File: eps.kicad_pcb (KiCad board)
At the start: 2 copper layers, 96 x 90 mm, 0 parts

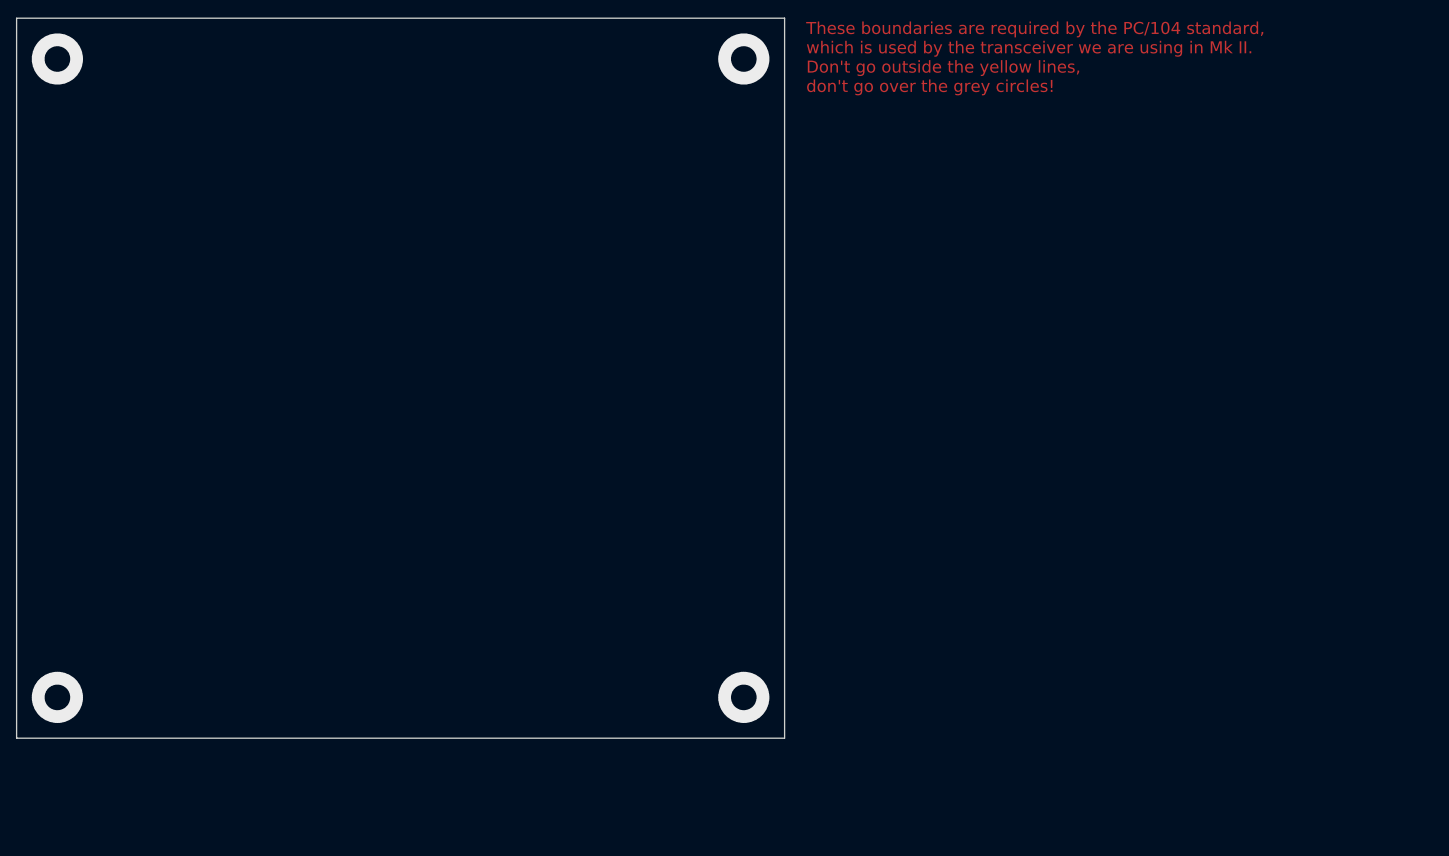
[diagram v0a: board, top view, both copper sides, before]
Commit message: PCB layout as of 2018-02-12
All that’s left to do is add deployment switches
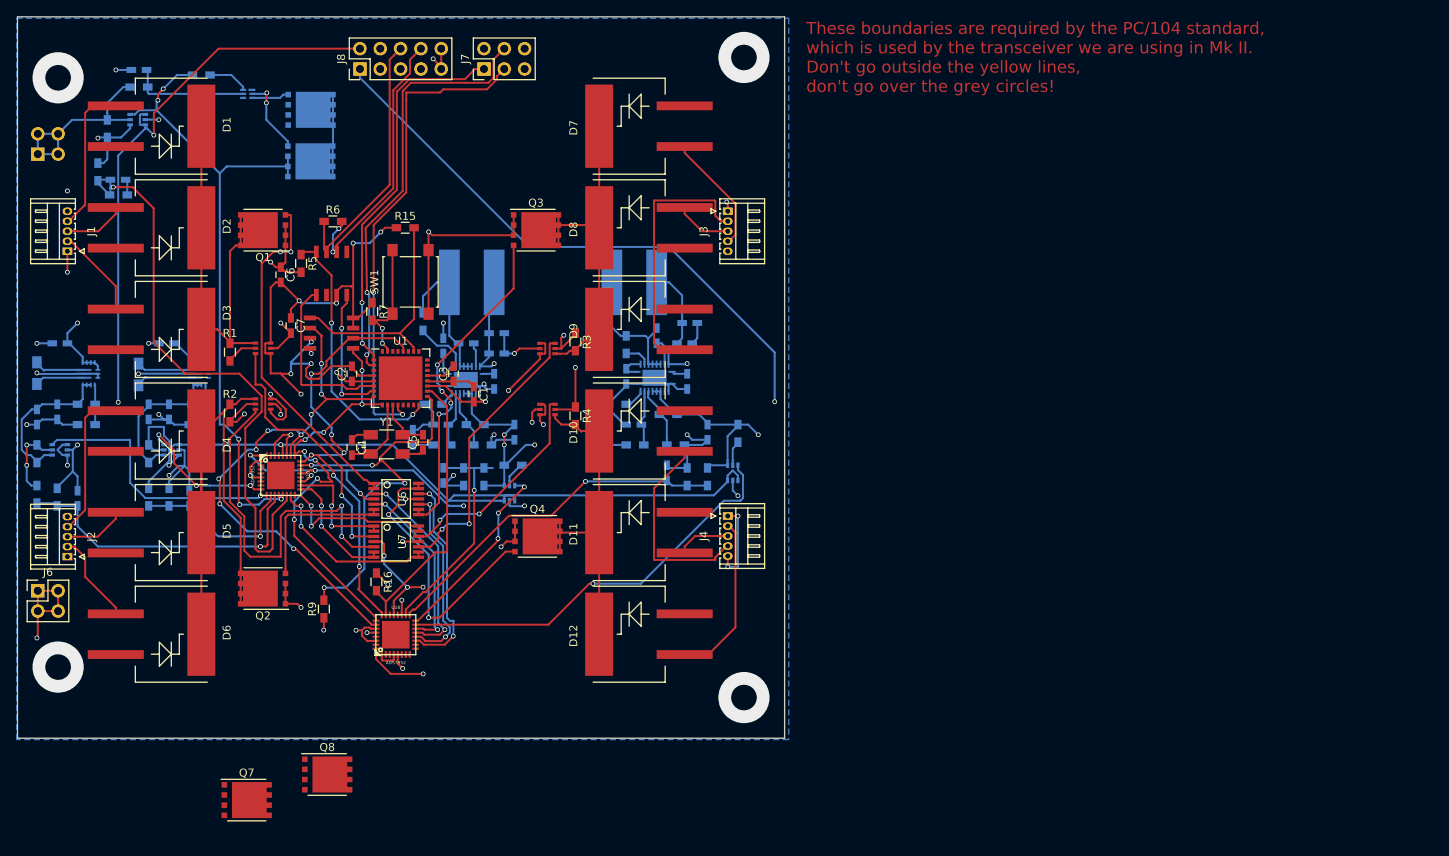
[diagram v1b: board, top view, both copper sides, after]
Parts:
- added C1: 0.1µF, Capacitors_SMD:C_0603_HandSoldering, F.Cu at (157.2, 97.0)
- added C10: C_Small, Capacitors_SMD:C_0603_HandSoldering, B.Cu at (121.6, 110.0)
- added C11: C_Small, Capacitors_SMD:C_0603_HandSoldering, B.Cu at (181.3, 106.8)
- added C12: C_Small, Capacitors_SMD:C_0603_HandSoldering, B.Cu at (153.3, 107.2)
- added C13: C_small, Capacitors_SMD:C_0603_HandSoldering, B.Cu at (112.7, 70.2)
- added C2: 0.1µF, Capacitors_SMD:C_0603_HandSoldering, F.Cu at (141.9, 94.5)
- added C3: 0.1µF, Capacitors_SMD:C_0603_HandSoldering, F.Cu at (154.6, 94.5)
- added C4: 22pF, Capacitors_SMD:C_0603_HandSoldering, F.Cu at (141.9, 103.7)
- added C5: 22pF, Capacitors_SMD:C_0603_HandSoldering, F.Cu at (150.8, 103.0)
- added C6: 0.1µF, Capacitors_SMD:C_0603_HandSoldering, F.Cu at (133.0, 82.1)
- added C7: 100nF, Capacitors_SMD:C_0603_HandSoldering, F.Cu at (134.3, 88.4)
- added C8: 0.1uF, Capacitors_SMD:C_0603_HandSoldering, B.Cu at (115.3, 56.5)
- added C9: C_Small, Capacitors_SMD:C_0603_HandSoldering, B.Cu at (107.6, 110.0)
- added CbstA1: 100nF, Capacitors_SMD:C_0603_HandSoldering, B.Cu at (156.2, 90.6)
- added CbstB1: 100nF, Capacitors_SMD:C_0603_HandSoldering, B.Cu at (180.0, 89.7)
- added Ccomp2A1: 82pF, Capacitors_SMD:C_0603_HandSoldering, B.Cu at (153.0, 100.8)
- added Ccomp2B1: 82pF, Capacitors_SMD:C_0603_HandSoldering, B.Cu at (177.2, 100.8)
- added CcompA1: 1.8nF, Capacitors_SMD:C_0603_HandSoldering, B.Cu at (149.5, 102.4)
- added CcompB1: 1.8nF, Capacitors_SMD:C_0603_HandSoldering, B.Cu at (173.7, 102.4)
- added Cin1: 10.0µF, Capacitors_SMD:C_0603_HandSoldering, B.Cu at (105.4, 90.6)
- added Cin2: 10.0µF, Capacitors_SMD:C_0603_HandSoldering, B.Cu at (118.7, 90.6)
- added Cin2A1: 100n, Capacitors_SMD:C_0603_HandSoldering, B.Cu at (160.0, 89.4)
- added Cin2B1: 100n, Capacitors_SMD:C_0603_HandSoldering, B.Cu at (184.1, 88.1)
- added CinA1: 12µF, Capacitors_SMD:C_0603_HandSoldering, B.Cu at (160.0, 91.9)
- added CinB1: 12µF, Capacitors_SMD:C_0603_HandSoldering, B.Cu at (183.5, 90.6)
- added Cout1: 47.0µF, Capacitors_SMD:C_0603_HandSoldering, B.Cu at (102.5, 99.8)
- added Cout2: 47.0µF, Capacitors_SMD:C_0603_HandSoldering, B.Cu at (116.5, 99.2)
- added CoutA1: 47µF, Capacitors_SMD:C_0603_HandSoldering, B.Cu at (162.2, 101.8)
- added CoutB1: 47µF, Capacitors_SMD:C_0603_HandSoldering, B.Cu at (186.4, 101.8)
- added Coutx1: 10.0µF, Capacitors_SMD:C_0603_HandSoldering, B.Cu at (105.1, 99.2)
- added Coutx2: 10.0µF, Capacitors_SMD:C_0603_HandSoldering, B.Cu at (119.0, 99.2)
- added CssA1: 8.2nF, Capacitors_SMD:C_0603_HandSoldering, B.Cu at (159.7, 95.4)
- added CssB1: 8.2nF, Capacitors_SMD:C_0603_HandSoldering, B.Cu at (183.8, 95.4)
- added CvccA1: 1µF, Capacitors_SMD:C_0603_HandSoldering, B.Cu at (153.3, 91.0)
- added CvccB1: 1µF, Capacitors_SMD:C_0603_HandSoldering, B.Cu at (176.2, 94.8)
- added D1: SM74611, Diodes_SMD:DD-PAK_TO263_SingleDiode, F.Cu at (116.8, 63.5)
- added D10: SM74611, Diodes_SMD:DD-PAK_TO263_SingleDiode, F.Cu at (179.1, 101.6)
- added D11: SM74611, Diodes_SMD:DD-PAK_TO263_SingleDiode, F.Cu at (179.1, 114.3)
- added D12: SM74611, Diodes_SMD:DD-PAK_TO263_SingleDiode, F.Cu at (179.1, 127.0)
- added D2: SM74611, Diodes_SMD:DD-PAK_TO263_SingleDiode, F.Cu at (116.8, 76.2)
- added D3: SM74611, Diodes_SMD:DD-PAK_TO263_SingleDiode, F.Cu at (116.8, 88.9)
- added D4: SM74611, Diodes_SMD:DD-PAK_TO263_SingleDiode, F.Cu at (116.8, 101.6)
- added D5: SM74611, Diodes_SMD:DD-PAK_TO263_SingleDiode, F.Cu at (116.8, 114.3)
- added D6: SM74611, Diodes_SMD:DD-PAK_TO263_SingleDiode, F.Cu at (116.8, 127.0)
- added D7: SM74611, Diodes_SMD:DD-PAK_TO263_SingleDiode, F.Cu at (179.1, 63.5)
- added D8: SM74611, Diodes_SMD:DD-PAK_TO263_SingleDiode, F.Cu at (179.1, 76.2)
- added D9: SM74611, Diodes_SMD:DD-PAK_TO263_SingleDiode, F.Cu at (179.1, 88.9)
- added J1: CONN_01X05, Connectors_Hirose:Hirose_DF13-05P-1.25DS_05x1.25mm_Angled, F.Cu at (106.3, 79.1)
- added J2: CONN_01X05, Connectors_Hirose:Hirose_DF13-05P-1.25DS_05x1.25mm_Angled, F.Cu at (106.3, 117.3)
- added J3: CONN_01X05, Connectors_Hirose:Hirose_DF13-05P-1.25DS_05x1.25mm_Angled, F.Cu at (188.9, 74.1)
- added J4: CONN_01X05, Connectors_Hirose:Hirose_DF13-05P-1.25DS_05x1.25mm_Angled, F.Cu at (188.9, 112.2)
- added J5: +BATT, Pin_Headers:Pin_Header_Straight_2x02_Pitch2.54mm, B.Cu at (102.7, 67.0)
- added J6: -BATT, Pin_Headers:Pin_Header_Straight_2x02_Pitch2.54mm, F.Cu at (102.7, 121.6)
- added J7: PROGRAMMING PORT, Pin_Headers:Pin_Header_Straight_2x03_Pitch2.54mm, F.Cu at (158.4, 56.4)
- added J8: H_EPS, Pin_Headers:Pin_Header_Straight_2x05_Pitch2.54mm, F.Cu at (142.9, 56.4)
- added L1: 1.0µH, Inductors_SMD:L_Vishay_IHLP-1212, B.Cu at (102.5, 94.4)
- added L2: 1.0µH, Inductors_SMD:L_Vishay_IHLP-1212, B.Cu at (115.2, 94.5)
- added LA1: 2.2µH, eps-libraries:SRN8040, B.Cu at (156.9, 83.0)
- added LB1: 2.2µH, eps-libraries:SRN8040, B.Cu at (177.2, 83.0)
- added Q1: BSC026NE2LS5, Housings_SON:VSONP-8-1EP_5x6_Pitch1.27mm, F.Cu at (130.8, 76.5)
- added Q2: BSC026NE2LS5, Housings_SON:VSONP-8-1EP_5x6_Pitch1.27mm, F.Cu at (130.8, 121.3)
- added Q3: BSC026NE2LS5, Housings_SON:VSONP-8-1EP_5x6_Pitch1.27mm, F.Cu at (164.9, 76.5)
- added Q4: BSC026NE2LS5, Housings_SON:VSONP-8-1EP_5x6_Pitch1.27mm, F.Cu at (165.1, 114.8)
- added Q5: BSC026NE2LS5, Housings_SON:VSONP-8-1EP_5x6_Pitch1.27mm, B.Cu at (136.7, 67.9)
- added Q6: BSC026NE2LS5, Housings_SON:VSONP-8-1EP_5x6_Pitch1.27mm, B.Cu at (136.7, 61.5)
- added Q7: BSC026NE2LS5, Housings_SON:VSONP-8-1EP_5x6_Pitch1.27mm, F.Cu at (128.8, 147.7)
- added Q8: BSC026NE2LS5, Housings_SON:VSONP-8-1EP_5x6_Pitch1.27mm, F.Cu at (138.8, 144.5)
- added R1: 10mΩ, Resistors_SMD:R_0603_HandSoldering, F.Cu at (126.7, 91.7)
- added R10: R_Small, Resistors_SMD:R_0603_HandSoldering, B.Cu at (105.1, 109.9)
- added R11: 2.2k, Resistors_SMD:R_0603_HandSoldering, B.Cu at (123.1, 57.1)
- added R12: 330, Resistors_SMD:R_0603_HandSoldering, B.Cu at (115.3, 58.6)
- added R13: 10kΩ, Resistors_SMD:R_0603_HandSoldering, B.Cu at (111.3, 63.8)
- added R14: R_Small, Resistors_SMD:R_0603_HandSoldering, B.Cu at (102.5, 109.5)
- added R15: 10k, Resistors_SMD:R_0603_HandSoldering, F.Cu at (148.6, 76.2)
- added R16: 10k, Resistors_SMD:R_0603_HandSoldering, F.Cu at (145.0, 120.5)
- added R17: 10m, Resistors_SMD:R_0603_HandSoldering, B.Cu at (162.1, 105.9)
- added R18: 10m, Resistors_SMD:R_0603_HandSoldering, B.Cu at (190.2, 101.9)
- added R19: R_Small, Resistors_SMD:R_0603_HandSoldering, B.Cu at (158.4, 107.3)
- added R2: 10mΩ, Resistors_SMD:R_0603_HandSoldering, F.Cu at (126.7, 99.4)
- added R20: R_Small, Resistors_SMD:R_0603_HandSoldering, B.Cu at (155.9, 107.3)
- added R23: R, Resistors_SMD:R_0603_HandSoldering, B.Cu at (110.2, 69.2)
- added R24: R, Resistors_SMD:R_0603_HandSoldering, B.Cu at (112.7, 72.1)
- added R25: 10mΩ, Resistors_SMD:R_0603_HandSoldering, B.Cu at (116.5, 104.4)
- added R26: R_Small, Resistors_SMD:R_0603_HandSoldering, B.Cu at (116.5, 109.9)
- added R27: R_Small, Resistors_SMD:R_0603_HandSoldering, B.Cu at (119.0, 109.9)
- added R28: R_Small, Resistors_SMD:R_0603_HandSoldering, B.Cu at (186.4, 107.3)
- added R29: R_Small, Resistors_SMD:R_0603_HandSoldering, B.Cu at (183.8, 107.3)
- added R3: 10mΩ, Resistors_SMD:R_0603_HandSoldering, F.Cu at (169.8, 90.5)
- added R4: 10mΩ, Resistors_SMD:R_0603_HandSoldering, F.Cu at (169.8, 99.7)
- added R5: 1kΩ, Resistors_SMD:R_0603_HandSoldering, F.Cu at (135.6, 80.7)
- added R6: 120Ω, Resistors_SMD:R_0603_HandSoldering, F.Cu at (139.5, 75.4)
- added R7: 10kΩ, Resistors_SMD:R_0603_HandSoldering, F.Cu at (144.4, 86.7)
- added R8: 10mΩ, Resistors_SMD:R_0603_HandSoldering, B.Cu at (102.5, 104.4)
- added R9: 10k, Resistors_SMD:R_0603_HandSoldering, F.Cu at (138.4, 123.8)
- added RcompA1: 15.8kΩ, Resistors_SMD:R_0603_HandSoldering, B.Cu at (153.2, 103.3)
- added RcompB1: 15.8kΩ, Resistors_SMD:R_0603_HandSoldering, B.Cu at (177.3, 103.3)
- added Rfbb1: 180k, Resistors_SMD:R_0603_HandSoldering, B.Cu at (108.7, 100.8)
- added Rfbb2: 180k, Resistors_SMD:R_0603_HandSoldering, B.Cu at (122.7, 100.8)
- added RfbbA1: 69.8kΩ, Resistors_SMD:R_0603_HandSoldering, B.Cu at (158.2, 103.3)
- added RfbbB1: 69.8kΩ, Resistors_SMD:R_0603_HandSoldering, B.Cu at (182.4, 103.3)
- added Rfbt1: 562k, Resistors_SMD:R_0603_HandSoldering, B.Cu at (108.7, 98.3)
- added Rfbt2: 562k, Resistors_SMD:R_0603_HandSoldering, B.Cu at (123.0, 98.3)
- added RfbtA1: 220k, Resistors_SMD:R_0603_HandSoldering, B.Cu at (157.3, 100.8)
- added RfbtB1: 220k, Resistors_SMD:R_0603_HandSoldering, B.Cu at (181.4, 99.5)
- added RlimA1: 162kΩ, Resistors_SMD:R_0603_HandSoldering, B.Cu at (152.1, 98.3)
- added RlimB1: 162kΩ, Resistors_SMD:R_0603_HandSoldering, B.Cu at (175.1, 98.3)
- added RtA1: 267kΩ, Resistors_SMD:R_0603_HandSoldering, B.Cu at (150.8, 87.9)
- added RtB1: 267kΩ, Resistors_SMD:R_0603_HandSoldering, B.Cu at (176.2, 90.8)
- added SW1: SW_RST, Buttons_Switches_SMD:SW_SPST_B3S-1000, F.Cu at (149.2, 83.0)
- added U1: ATMEGA32M1-MU, Housings_DFN_QFN:QFN-32-1EP_7x7mm_Pitch0.65mm, F.Cu at (148.0, 95.0)
- added U10: ADS7952, w_smd_qfn:pvqfn-n32, F.Cu at (133.0, 107.2)
- added U11: TPS630250, eps:VQFN-14, B.Cu at (109.0, 94.5)
- added U12: bq297xx, Housings_SON:WSON6_1.5x1.5mm_Pitch0.5mm, B.Cu at (128.9, 59.5)
- added U13: INA214, kicad-libraries:SC70-6, B.Cu at (115.1, 62.7)
- added U14: INA214, kicad-libraries:SC70-6, B.Cu at (105.4, 104.0)
- added U15: TPS630250, eps:VQFN-14, B.Cu at (122.9, 94.5)
- added U16: TPS61088, w_smd_qfn:pvqfn-n20, B.Cu at (156.1, 95.2)
- added U17: TPS61088, w_smd_qfn:pvqfn-n20, B.Cu at (179.7, 95.0)
- added U18: ADS7952, w_smd_qfn:pvqfn-n32, F.Cu at (147.4, 127.1)
- added U19: INA214, kicad-libraries:SC70-6, B.Cu at (119.4, 104.0)
- added U2: INA214, kicad-libraries:SC70-6, F.Cu at (130.8, 91.3)
- added U20: INA214, kicad-libraries:SC70-6, B.Cu at (161.6, 109.4)
- added U21: INA214, kicad-libraries:SC70-6, B.Cu at (189.5, 106.8)
- added U3: INA214, kicad-libraries:SC70-6, F.Cu at (130.8, 98.2)
- added U4: INA214, kicad-libraries:SC70-6, F.Cu at (166.4, 91.3)
- added U5: INA214, kicad-libraries:SC70-6, F.Cu at (166.4, 98.9)
- added U6: ADA4891-4, SMD_Packages:SSOP-14, F.Cu at (147.5, 110.1)
- added U7: ADA4891-4, SMD_Packages:SSOP-14, F.Cu at (147.5, 115.4)
- added U8: SN65HVD230, kicad-libraries:SOIC8, F.Cu at (139.4, 81.9)
- added U9: SST25VF016B, kicad-libraries:SOIC8, F.Cu at (139.4, 89.4)
- added Y1: 8MHz, Crystals:Crystal_SMD_Abracon_ABM3B-4pin_5.0x3.2mm, F.Cu at (146.3, 103.3)
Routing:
- net +3V3: track 0.00 -> 302.7 mm, vias 0 -> 22
- net GND: track 0.00 -> 264.0 mm, vias 0 -> 50
- net +5V: track 0.00 -> 140.9 mm, vias 0 -> 9
- net -PACK: track 0.00 -> 83.4 mm, vias 0 -> 5
- net +PACK: track 0.00 -> 79.7 mm, vias 0 -> 7
- net Net-(D4-Pad2): track 0.00 -> 75.5 mm
- net /VPACK: track 0.00 -> 72.8 mm, vias 0 -> 1
- net /MISO: track 0.00 -> 67.7 mm, vias 0 -> 9
- net /SCK_A: track 0.00 -> 60.6 mm, vias 0 -> 2
- net /SCK: track 0.00 -> 56.3 mm, vias 0 -> 6
- net /MOSI: track 0.00 -> 54.6 mm, vias 0 -> 8
- net /MOSI_A: track 0.00 -> 53.5 mm, vias 0 -> 2
- net Net-(D1-Pad2): track 0.00 -> 52.7 mm
- net /IOUTB: track 0.00 -> 51.8 mm, vias 0 -> 1
- net /CS_ADC1: track 0.00 -> 50.1 mm, vias 0 -> 4
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- added copper zone on VCC, net +3V3
- added copper zone on VCC, net +5V
- added copper zone on VCC, net +PACK
- added copper zone on B.Cu, net GND
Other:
- board size 96 x 90 mm -> 95.9 x 90.2 mm
- copper layers 2 -> 4

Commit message: Refilled pours
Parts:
- removed Q7, Q8: BSC026NE2LS5, Housings_SON:VSONP-8-1EP_5x6_Pitch1.27mm

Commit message: Added deployment/RBL switches and debug headers to EPS board
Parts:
- added J9: DEBUG, Pin_Headers:Pin_Header_Straight_2x04_Pitch2.54mm, F.Cu at (130.5, 56.4)
- added Q7, Q8: BSC026NE2LS5, Housings_SON:VSONP-8-1EP_5x6_Pitch1.27mm, F.Cu at (148.1, 150.1)
- added S1: DEP. SWITCH, Connectors_Hirose:Hirose_DF13-02P-1.25DS_02x1.25mm_Angled, F.Cu at (106.3, 86.8)
- added S2: DEP. SWITCH, Connectors_Hirose:Hirose_DF13-02P-1.25DS_02x1.25mm_Angled, F.Cu at (106.3, 93.2)
- added S3: DEP. SWITCH, Connectors_Hirose:Hirose_DF13-02P-1.25DS_02x1.25mm_Angled, F.Cu at (106.3, 100.8)
- added S4: RBL PIN, Connectors_Hirose:Hirose_DF13-02P-1.25DS_02x1.25mm_Angled, F.Cu at (106.3, 107.1)
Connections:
- J6 pad 1: GND -> Net-(J6-Pad1)
- J6 pad 2: GND -> Net-(J6-Pad1)
- J6 pad 3: GND -> Net-(J6-Pad1)
- J6 pad 4: GND -> Net-(J6-Pad1)
- R12 pad 1: Net-(J5-Pad1) -> Net-(R12-Pad1)
- R13 pad 1: Net-(J5-Pad1) -> Net-(R12-Pad1)
- U1 pad 12: /SCK_A -> Net-(U1-Pad12)
- U1 pad 2: /MOSI_A -> Net-(U1-Pad2)
- U13 pad 5: Net-(J5-Pad1) -> Net-(R12-Pad1)
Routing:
- net Net-(R12-Pad1): track 0.00 -> 42.0 mm, vias 0 -> 1
- net Net-(J6-Pad1): track 0.00 -> 25.2 mm
- net Net-(U1-Pad2): track 0.00 -> 24.8 mm, vias 0 -> 2
- net Net-(U1-Pad12): track 0.00 -> 20.2 mm, vias 0 -> 1
- net Net-(J5-Pad1): track 25.7 -> 40.4 mm
- net +3V3: track 302.7 -> 292.8 mm, vias 22 -> 21
- net Net-(S1-Pad1): track 0.00 -> 7.31 mm
- net +5V: track 140.9 -> 146.8 mm
- net +PACK: track 79.7 -> 84.9 mm, vias 7 -> 8
- net Net-(S3-Pad1): track 0.00 -> 4.45 mm, vias 0 -> 1
- net /MOSI_A: track 53.5 -> 49.1 mm
- net GND: track 264.0 -> 260.7 mm, vias 50 -> 52
- net /SCK_A: track 60.6 -> 59.7 mm, vias 2 -> 3

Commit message: Replaced battery connectors with DF13
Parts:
- removed Q7, Q8: BSC026NE2LS5, Housings_SON:VSONP-8-1EP_5x6_Pitch1.27mm
- J5: footprint Pin_Headers:Pin_Header_Straight_2x02_Pitch2.54mm -> Connectors_Hirose:Hirose_DF13-04P-1.25DS_04x1.25mm_Angled; moved to F.Cu
- J6: footprint Pin_Headers:Pin_Header_Straight_2x02_Pitch2.54mm -> Connectors_Hirose:Hirose_DF13-04P-1.25DS_04x1.25mm_Angled
- moved J6 5.26 mm to (106.3, 125.3), turned to 90 degrees
- moved J5 4.69 mm to (106.3, 69.9), turned to 90 degrees
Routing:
- net Net-(U1-Pad2): track 24.8 -> 2.41 mm, vias 2 -> 1
- net /MOSI_A: track 49.1 -> 71.5 mm, vias 2 -> 3
- net Net-(R12-Pad1): track 42.0 -> 62.6 mm, vias 1 -> 2
- net /SCK_A: track 59.7 -> 79.3 mm, vias 3 -> 4
- net Net-(U1-Pad12): track 20.2 -> 0.59 mm, vias 1 -> 0
- net Net-(J6-Pad1): track 25.2 -> 19.2 mm
- net Net-(J5-Pad1): track 40.4 -> 35.4 mm

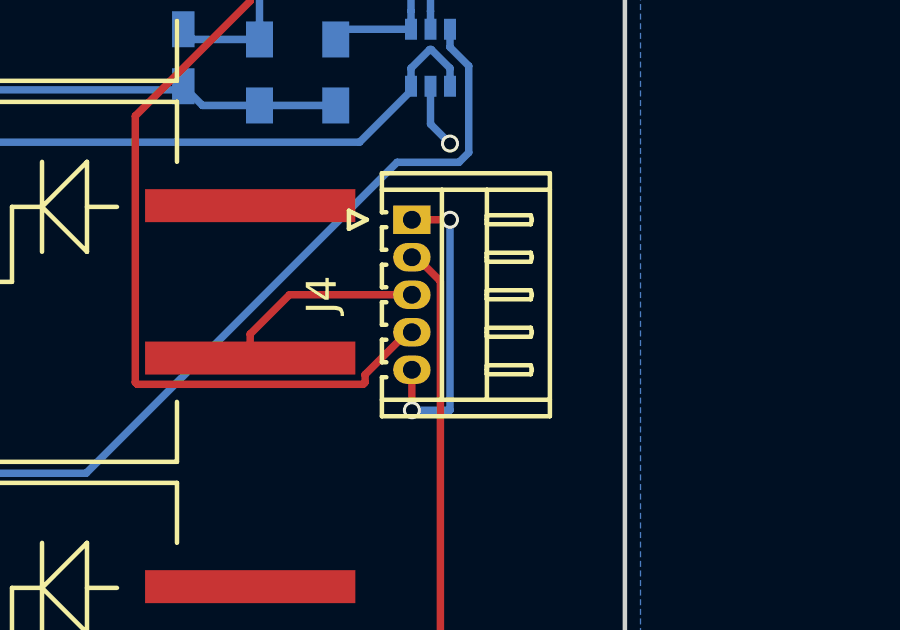
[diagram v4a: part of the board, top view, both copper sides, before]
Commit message: fixed gnd pour over corner holes
I think I didn't break anything
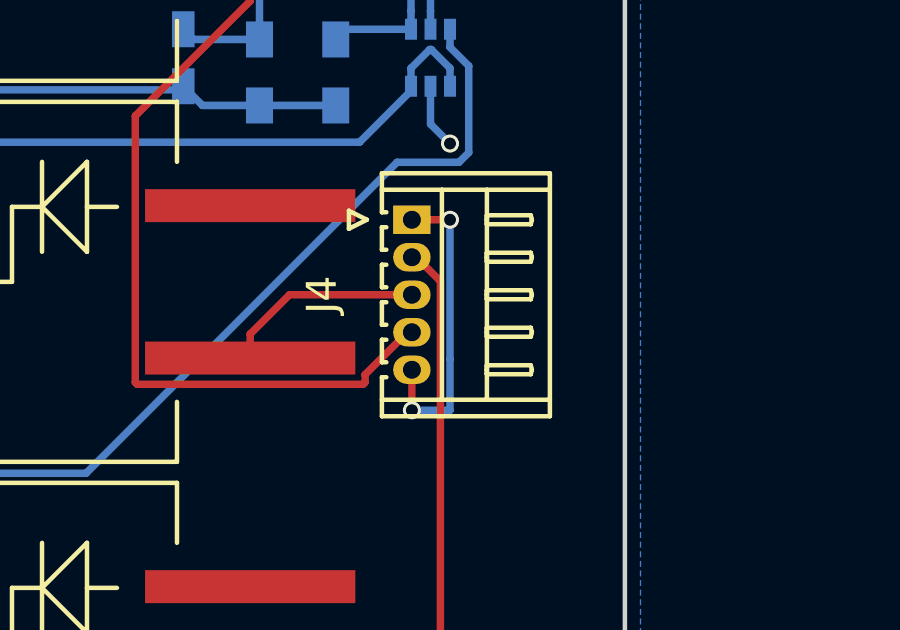
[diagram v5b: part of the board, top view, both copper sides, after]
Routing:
- net GND: vias 52 -> 54
- net (no net): vias 4 -> 2
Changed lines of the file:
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@@
     (links 448)
     (no_connects 49)
-    (area 100.034999 49.754999 196.075001 140.075001)
+    (area 98.589999 47.237143 263.414284 141.520002)
     (thickness 1.6)
     (drawings 5)
-    (tracks 1621)
+    (tracks 1622)
     (zones 0)
     (modules 134)
@@
     (via_min_size 0.4)
     (via_min_drill 0.3)
+    (user_via 5.4 3.2)
     (user_via 6.4 3.2)
     (uvia_size 0.3)
@@
     (pad_to_mask_clearance 0.2)
     (aux_axis_origin 0 0)
-    (grid_origin 100 50)
+    (grid_origin 187.95 54.93)
     (visible_elements 7FFFFFFF)
     (pcbplotparams
@@
   (via (at 190.92 134.92) (size 6.4) (drill 3.2) (layers F.Cu B.Cu) (net 0))
   (via (at 105.19 131.11) (size 6.4) (drill 3.2) (layers F.Cu B.Cu) (net 0))
-  (via (at 105.19 57.45) (size 6.4) (drill 3.2) (layers F.Cu B.Cu) (net 0))
-  (via (at 190.92 54.91) (size 6.4) (drill 3.2) (layers F.Cu B.Cu) (net 0))
+  (via (at 190.92 54.91) (size 6.4) (drill 3.2) (layers F.Cu B.Cu) (net 1))
+  (via (at 105.19 57.45) (size 6.4) (drill 3.2) (layers F.Cu B.Cu) (net 1))
   (segment (start 130.48 53.81) (end 129.21 53.81) (width 0.25) (layer F.Cu) (net 1))
   (segment (start 129.21 53.81) (end 127.94 52.54) (width 0.25) (layer F.Cu) (net 1))
@@
   (via (at 188.9 74.13) (size 0.6) (drill 0.4) (layers F.Cu B.Cu) (net 1))
   (segment (start 190.17 112.23) (end 188.9 112.23) (width 0.25) (layer F.Cu) (net 1))
-  (segment (start 190.17 118.58) (end 190.17 112.23) (width 0.25) (layer B.Cu) (net 1))
+  (segment (start 190.17 118.58) (end 190.17 116.88) (width 0.25) (layer B.Cu) (net 1))
+  (segment (start 190.17 116.88) (end 190.17 112.23) (width 0.25) (layer B.Cu) (net 1))
   (via (at 190.17 112.23) (size 0.6) (drill 0.4) (layers F.Cu B.Cu) (net 1))
   (segment (start 188.9 118.58) (end 190.17 118.58) (width 0.25) (layer B.Cu) (net 1))

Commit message: Exported EPS board
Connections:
- R7 pad 2: Net-(R7-Pad2) -> /EPS_RST
- SW1 pad 1: Net-(R7-Pad2) -> /EPS_RST
- U1 pad 31: Net-(R7-Pad2) -> /EPS_RST
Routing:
- net +3V3: track 292.8 -> 422.4 mm, vias 21 -> 20
- net /EPS_RST: track 0.00 -> 68.3 mm, vias 0 -> 2
- net GND: track 260.7 -> 295.6 mm, vias 54 -> 52
- net Net-(R7-Pad2): track 15.8 -> 0.00 mm, vias 2 -> 0
- net +5V: track 146.8 -> 155.3 mm
- net (no net): vias 2 -> 4

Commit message: Save checkpoint
Deleted warning text. If anything dies please revert to this version!
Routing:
- net Net-(S3-Pad1): track 4.45 -> 5.08 mm
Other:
- board text removed: "These boundaries are required by the PC/104 standard, which is used by the transceiver we are using in Mk II. Don't go outside the yellow lines, don't go over the grey circles!"
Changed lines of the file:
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@@
     (area 98.589999 47.237143 263.414284 141.520002)
     (thickness 1.6)
-    (drawings 5)
-    (tracks 1686)
+    (drawings 4)
+    (tracks 1687)
     (zones 0)
     (modules 134)
@@
   (gr_line (start 196 49.83) (end 100.11 49.83) (angle 90) (layer Edge.Cuts) (width 0.15))
   (gr_line (start 196 49.83) (end 196 140) (angle 90) (layer Edge.Cuts) (width 0.15))
-  (gr_text "These boundaries are required by the PC/104 standard,\nwhich is used by the transceiver we are using in Mk II.\nDon't go outside the yellow lines, \ndon't go over the grey circles!\n" (at 198.7 54.9) (layer F.Cu)
-    (effects (font (size 1.5 1.5) (thickness 0.3)) (justify left))
-  )
   (via (at 190.92 54.91) (size 6.4) (drill 3.2) (layers F.Cu B.Cu) (net 0))
   (via (at 190.92 134.92) (size 6.4) (drill 3.2) (layers F.Cu B.Cu) (net 0))
@@
   (segment (start 108.245001 87.799999) (end 107.255002 86.81) (width 0.25) (layer F.Cu) (net 145))
   (segment (start 107.225 86.81) (end 106.35 86.81) (width 0.25) (layer F.Cu) (net 145))
+  (segment (start 106.35 105.254999) (end 106.35 105.88) (width 0.25) (layer F.Cu) (net 146))
   (via (at 106.35 105.88) (size 0.6) (drill 0.4) (layers F.Cu B.Cu) (net 146))
   (segment (start 106.35 100.8) (end 106.35 105.254999) (width 0.25) (layer F.Cu) (net 146))
